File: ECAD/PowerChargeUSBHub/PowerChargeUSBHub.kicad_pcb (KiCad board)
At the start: 2 copper layers, 0 parts

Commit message: WIP - first components
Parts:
- added D1: LED_Small, LED_THT:LED_D5.0mm_Horizontal_O1.27mm_Z3.0mm, F.Cu at (220.3, 66.5)
- added D2: 1N5817, Diode_THT:D_DO-41_SOD81_P10.16mm_Horizontal, F.Cu at (209.0, 74.9)
- added D3: 1N5817, Diode_THT:D_DO-41_SOD81_P10.16mm_Horizontal, F.Cu at (172.0, 74.9)
- added D4: 1N5817, Diode_THT:D_DO-41_SOD81_P10.16mm_Horizontal, F.Cu at (191.0, 75.0)
- added H1: M3, MountingHole:MountingHole_3.2mm_M3_Pad_Via, F.Cu at (159.4, 79.0)
- added H2: M3, MountingHole:MountingHole_3.2mm_M3_Pad_Via, F.Cu at (225.0, 79.0)
- added J1: USB_A, Connector_USB:USB_A_Molex_67643_Horizontal, F.Cu at (172.5, 70.0)
- added J2: USB_A, Connector_USB:USB_A_Molex_67643_Horizontal, F.Cu at (190.5, 70.0)
- added J3: USB_A, Connector_USB:USB_A_Molex_67643_Horizontal, F.Cu at (208.5, 70.0)
- added JP1: SolderJumper_2_Open, Jumper:SolderJumper-2_P1.3mm_Open_Pad1.0x1.5mm, F.Cu at (209.0, 80.0)
- added JP2: SolderJumper_2_Open, Jumper:SolderJumper-2_P1.3mm_Open_Pad1.0x1.5mm, F.Cu at (172.0, 80.0)
- added JP3: SolderJumper_2_Open, Jumper:SolderJumper-2_P1.3mm_Open_Pad1.0x1.5mm, F.Cu at (191.0, 80.1)
- added R1: R_Small, Resistor_SMD:R_1206_3216Metric_Pad1.30x1.75mm_HandSolder, F.Cu at (217.4, 71.0)
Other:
- board outline added: 74 x 30 mm

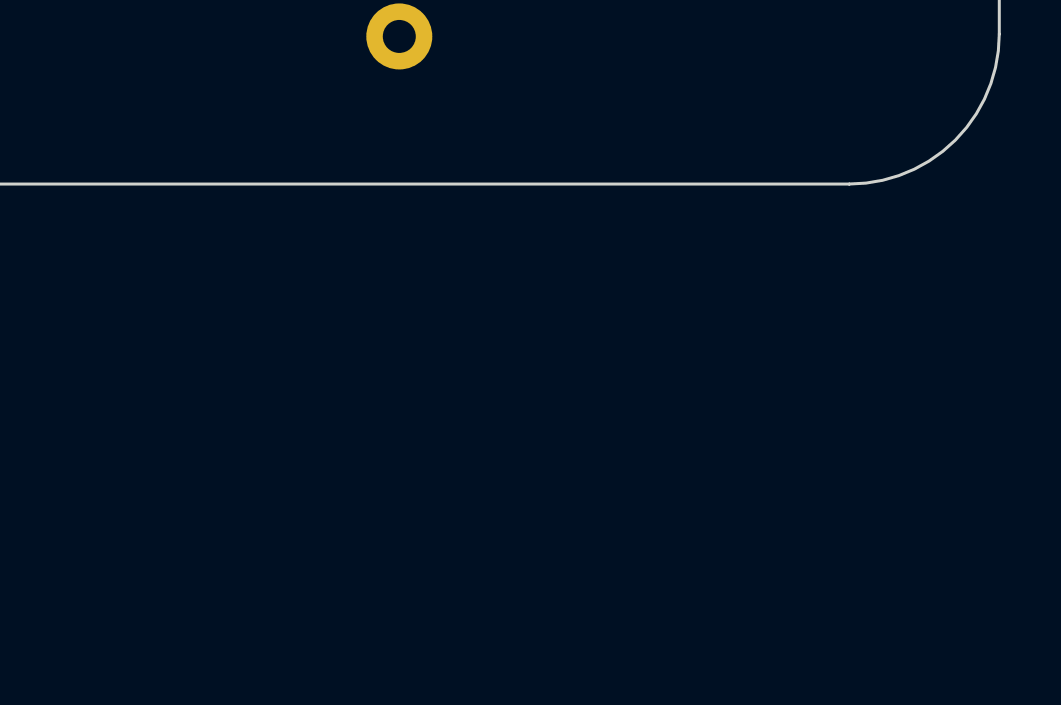
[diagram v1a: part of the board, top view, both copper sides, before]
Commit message: Add usbn C and polyfuse
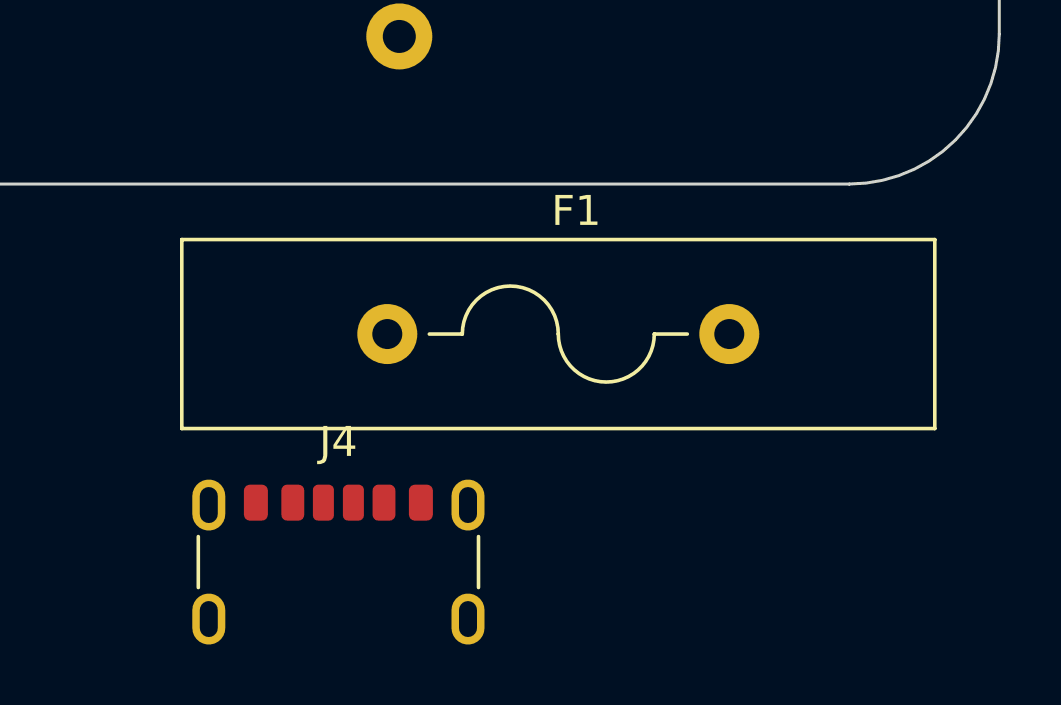
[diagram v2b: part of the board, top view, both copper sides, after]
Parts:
- added F1: Polyfuse_Small, PCM_Fuse_US_AKL:Fuse_Littelfuse-LVR200, F.Cu at (208.6, 95.0)
- added J4: USB_C_Receptacle_PowerOnly_6P, Connector_USB:USB_C_Receptacle_GCT_USB4125-xx-x_6P_TopMnt_Horizontal, F.Cu at (207.0, 103.7)
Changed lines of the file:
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@@
   (net 11 "Net-(D4-K)")
   (net 12 "Net-(D1-A)")
+  (net 13 "Net-(F1-Pad1)")
+  (net 14 "unconnected-(J4-CC1-PadA5)")
+  (net 15 "unconnected-(J4-CC2-PadB5)")
+  (footprint "Connector_USB:USB_C_Receptacle_GCT_USB4125-xx-x_6P_TopMnt_Horizontal" (layer "F.Cu")
+    (at 206.97 103.7)
+    (descr "USB Type C Receptacle, GCT, power-only, 6P, top mounted, horizontal, 3A, 1mm stake: https://gct.co/files/drawings/usb4125.pdf")
+    (tags "USB C Type-C receptacle power-only charging-only 6P 6C right angled")
+    (property "Sheetfile" "PowerChargeUSBHub.kicad_sch")
+    (property "Sheetname" "")
+    (property "ki_description" "USB Power-Only 6P Type-C Receptacle connector")
+    (property "ki_keywords" "usb universal serial bus type-C power-only charging-only 6P 6C")
+    (attr smd)
+    (fp_text reference "J4" (at 0 -5.1 unlocked) (layer "F.SilkS")
+        (effects (font (size 1 1) (thickness 0.15)))
+    )
+    (fp_text value "USB_C_Receptacle_PowerOnly_6P" (at 0 4.725 unlocked) (layer "F.Fab")
+        (effects (font (size 1 1) (thickness 0.15)))
+    )
+    (fp_text user "PCB Edge" (at 0 2.825 unlocked) (layer "Dwgs.User")
+        (effects (font (size 0.5 0.5) (thickness 0.1)))
+    )
+    (fp_text user "${REFERENCE}" (at 0 -0.275 unlocked) (layer "F.Fab")
+        (effects (font (size 1 1) (thickness 0.15)))
+    )
+    (fp_line (start -4.67 -0.25) (end -4.67 -1.95)
+      (stroke (width 0.12) (type solid)) (layer "F.SilkS"))
+    (fp_line (start 4.67 -0.25) (end 4.67 -1.95)
+      (stroke (width 0.12) (type solid)) (layer "F.SilkS"))
+    (fp_line (start 5 3.4) (end -5 3.4)
+      (stroke (width 0.1) (type solid)) (layer "Dwgs.User"))
+    (fp_rect (start -5.37 -4.35) (end 5.37 3.9)
+      (stroke (width 0.05) (type solid)) (fill none) (layer "F.CrtYd"))
+    (fp_rect (start -4.47 -3.4) (end 4.47 3.4)
+      (stroke (width 0.1) (type solid)) (fill none) (layer "F.Fab"))
+    (pad "A5" smd roundrect (at -0.5 -3.08) (size 0.7 1.2) (layers "F.Cu" "F.Paste" "F.Mask") (roundrect_rratio 0.25)
+      (net 14 "unconnected-(J4-CC1-PadA5)") (pinfunction "CC1") (pintype "bidirectional+no_connect"))
+    (pad "A9" smd roundrect (at 1.52 -3.08 180) (size 0.76 1.2) (layers "F.Cu" "F.Paste" "F.Mask") (roundrect_rratio 0.25)
+      (net 13 "Net-(F1-Pad1)") (pinfunction "VBUS") (pintype "passive"))
+    (pad "A12" smd roundrect (at 2.75 -3.08 180) (size 0.8 1.2) (layers "F.Cu" "F.Paste" "F.Mask") (roundrect_rratio 0.25)
+      (net 4 "GND") (pinfunction "GND") (pintype "passive"))
+    (pad "B5" smd roundrect (at 0.5 -3.08 180) (size 0.7 1.2) (layers "F.Cu" "F.Paste" "F.Mask") (roundrect_rratio 0.25)
+      (net 15 "unconnected-(J4-CC2-PadB5)") (pinfunction "CC2") (pintype "bidirectional+no_connect"))
+    (pad "B9" smd roundrect (at -1.52 -3.08) (size 0.76 1.2) (layers "F.Cu" "F.Paste" "F.Mask") (roundrect_rratio 0.25)
+      (net 13 "Net-(F1-Pad1)") (pinfunction "VBUS") (pintype "passive"))
+    (pad "B12" smd roundrect (at -2.75 -3.08) (size 0.8 1.2) (layers "F.Cu" "F.Paste" "F.Mask") (roundrect_rratio 0.25)
+      (net 4 "GND") (pinfunction "GND") (pintype "passive"))
+    (pad "S1" thru_hole oval (at -4.32 -3) (size 1.1 1.7) (drill oval 0.6 1.2) (layers "*.Cu" "*.Mask" "F.Paste")
+      (net 4 "GND") (pinfunction "SHIELD") (pintype "passive"))
+    (pad "S1" thru_hole oval (at -4.32 0.8) (size 1.1 1.7) (drill oval 0.6 1.2) (layers "*.Cu" "*.Mask" "F.Paste")
+      (net 4 "GND") (pinfunction "SHIELD") (pintype "passive"))
+    (pad "S1" thru_hole oval (at 4.32 -3) (size 1.1 1.7) (drill oval 0.6 1.2) (layers "*.Cu" "*.Mask" "F.Paste")
+      (net 4 "GND") (pinfunction "SHIELD") (pintype "passive"))
+    (pad "S1" thru_hole oval (at 4.32 0.8) (size 1.1 1.7) (drill oval 0.6 1.2) (layers "*.Cu" "*.Mask" "F.Paste")
+      (net 4 "GND") (pinfunction "SHIELD") (pintype "passive"))
+    (model "${KICAD7_3DMODEL_DIR}/Connector_USB.3dshapes/USB_C_Receptacle_GCT_USB4125-xx-x_6P_TopMnt_Horizontal.wrl"
+      (offset (xyz 0 0 0))
+      (scale (xyz 1 1 1))
+      (rotate (xyz 0 0 0))
+    )
+  )
+  (footprint "PCM_Fuse_US_AKL:Fuse_Littelfuse-LVR200" (layer "F.Cu")
+    (at 208.6 95)
+    (descr "Littelfuse, resettable fuse, PTC, polyswitch LVR200, Ih 2A, http://www.littelfuse.com/~/media/electronics/datasheets/resettable_ptcs/littelfuse_ptc_lvr_catalog_datasheet.pdf.pdf, Alternate KiCAD Library")
+    (tags "LVR200 PTC resettable polyswitch ")
+    (property "Sheetfile" "PowerChargeUSBHub.kicad_sch")
+    (property "Sheetname" "")
+    (property "ki_description" "Resettable fuse, polymeric positive temperature coefficient, small symbol")
+    (property "ki_keywords" "resettable fuse PTC PPTC polyfuse polyswitch")
+    (fp_text reference "F1" (at 6.3 -4.1) (layer "F.SilkS")
+        (effects (font (size 1 1) (thickness 0.15)))
+    )
+    (fp_text value "Polyfuse_Small" (at 5.5 4.2) (layer "F.Fab") hide
+        (effects (font (size 1 1) (thickness 0.15)))
+    )
+    (fp_text user "${REFERENCE}" (at 6 0) (layer "F.Fab")
+        (effects (font (size 1 1) (thickness 0.15)))
+    )
+    (fp_line (start -6.85 -3.15) (end -6.85 3.15)
+      (stroke (width 0.12) (type solid)) (layer "F.SilkS"))
+    (fp_line (start -6.85 -3.15) (end 18.25 -3.15)
+      (stroke (width 0.12) (type solid)) (layer "F.SilkS"))
+    (fp_line (start 1.4 0) (end 2.5 0)
+      (stroke (width 0.12) (type solid)) (layer "F.SilkS"))
+    (fp_line (start 8.9 0) (end 10 0)
+      (stroke (width 0.12) (type solid)) (layer "F.SilkS"))
+    (fp_line (start 18.25 3.15) (end -6.85 3.15)
+      (stroke (width 0.12) (type solid)) (layer "F.SilkS"))
+    (fp_line (start 18.25 3.15) (end 18.25 -3.15)
+      (stroke (width 0.12) (type solid)) (layer "F.SilkS"))
+    (fp_arc (start 2.5 0) (mid 4.1 -1.6) (end 5.7 0)
+      (stroke (width 0.12) (type solid)) (layer "F.SilkS"))
+    (fp_arc (start 8.9 0) (mid 7.3 1.6) (end 5.7 0)
+      (stroke (width 0.12) (type solid)) (layer "F.SilkS"))
+    (fp_line (start -7 -3.3) (end -7 3.3)
+      (stroke (width 0.05) (type solid)) (layer "F.CrtYd"))
+    (fp_line (start -7 -3.3) (end 18.4 -3.3)
+      (stroke (width 0.05) (type solid)) (layer "F.CrtYd"))
+    (fp_line (start 18.4 3.3) (end -7 3.3)
+      (stroke (width 0.05) (type solid)) (layer "F.CrtYd"))
+    (fp_line (start 18.4 3.3) (end 18.4 -3.3)
+      (stroke (width 0.05) (type solid)) (layer "F.CrtYd"))
+    (fp_line (start -6.75 -3.05) (end -6.75 3.05)
+      (stroke (width 0.1) (type solid)) (layer "F.Fab"))
+    (fp_line (start -6.75 3.05) (end 18.15 3.05)
+      (stroke (width 0.1) (type solid)) (layer "F.Fab"))
+    (fp_line (start 18.15 -3.05) (end -6.75 -3.05)
+      (stroke (width 0.1) (type solid)) (layer "F.Fab"))
+    (fp_line (start 18.15 3.05) (end 18.15 -3.05)
+      (stroke (width 0.1) (type solid)) (layer "F.Fab"))
+    (pad "1" thru_hole circle (at 0 0) (size 2 2) (drill 1) (layers "*.Cu" "*.Mask")
+      (net 13 "Net-(F1-Pad1)") (pintype "passive"))
+    (pad "2" thru_hole circle (at 11.4 0) (size 2 2) (drill 1) (layers "*.Cu" "*.Mask")
+      (net 1 "+5V") (pintype "passive"))
+  )
   (footprint "Connector_USB:USB_A_Molex_67643_Horizontal" (layer "F.Cu")
     (at 190.5 70 180)

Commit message: Create Dock
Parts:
- added H3: M3, MountingHole:MountingHole_3.2mm_M3_Pad_Via, F.Cu at (160.5, 80.0)
- added H4: M3, MountingHole:MountingHole_3.2mm_M3_Pad_Via, F.Cu at (223.5, 80.0)
- moved J4 27.0 mm to (181.2, 95.7)
- moved H2 25.0 mm to (223.5, 104.0)
- moved H1 25.0 mm to (160.5, 104.0)
- moved D3 18.5 mm to (190.5, 74.4)
- moved JP2 18.5 mm to (190.5, 79.5)
- moved D4 18.5 mm to (172.5, 74.6)
- moved JP3 18.5 mm to (172.5, 79.7)
- moved F1 4.80 mm to (203.8, 95.0)
- moved J1 1.14 mm to (172.5, 68.9)
- moved J2 1.14 mm to (190.5, 68.9)
- moved J3 1.14 mm to (208.5, 68.9)
- moved D2 0.61 mm to (208.5, 74.6)
- moved JP1 0.61 mm to (208.5, 79.7)
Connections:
- J1 pad 1: Net-(D3-K) -> Net-(D4-K)
- J2 pad 1: Net-(D4-K) -> Net-(D3-K)
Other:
- board size 74 x 30 mm -> 73 x 49 mm
